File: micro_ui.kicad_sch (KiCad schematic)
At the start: 1 part

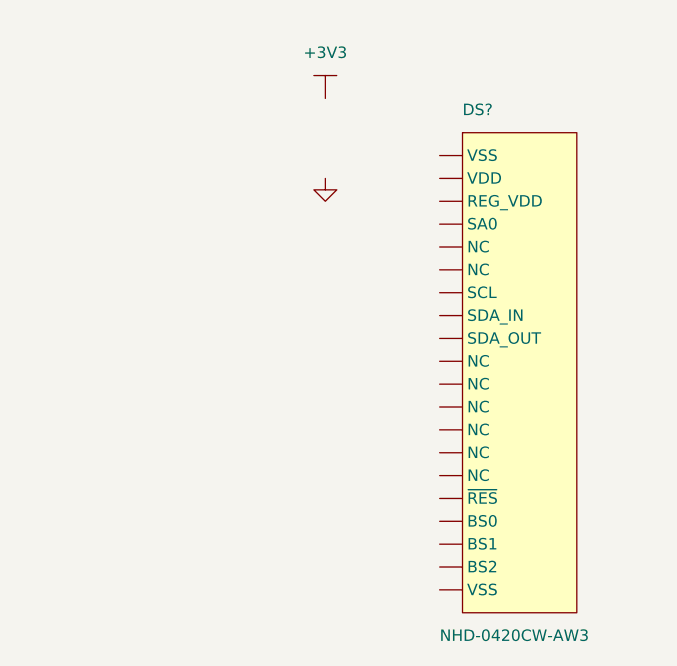
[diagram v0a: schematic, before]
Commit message: added symbols for i2c res and decoupling cap
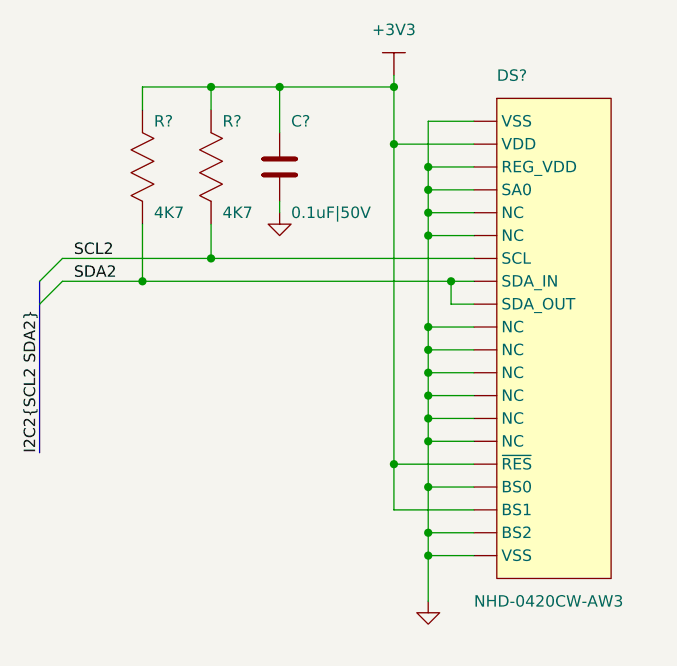
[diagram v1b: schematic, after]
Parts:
- added C?: 0.1uF|50V, symbol tbc:GCJ188R71H104KA12D
- added R? (x2): 4K7, symbol tbc:RC0603FR-074K7L
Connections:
- net +3V3: now also DS?.16 (~{RES}), DS?.18 (BS1), DS?.2 (VDD), C?.2, R?.2, R?.2
- net GND: now also DS?.1 (VSS), DS?.10 (DB3), DS?.11 (DB4), DS?.12 (DB5), DS?.13 (DB6), DS?.14 (DB7), DS?.15 (~{CS}), DS?.17 (BS0), DS?.19 (BS2), DS?.20 (VSS), DS?.3 (REG_VDD), DS?.4 (D_C), DS?.5 (R_W), DS?.6 (E), C?.1
- net SCL2: now reaches DS?.7 (DB0)
- net SCL2: now also R?.1
- net SDA2: now reaches DS?.8 (DB1)
- net SDA2: now also DS?.9 (DB2), R?.1
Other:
- moved on the sheet: DS?

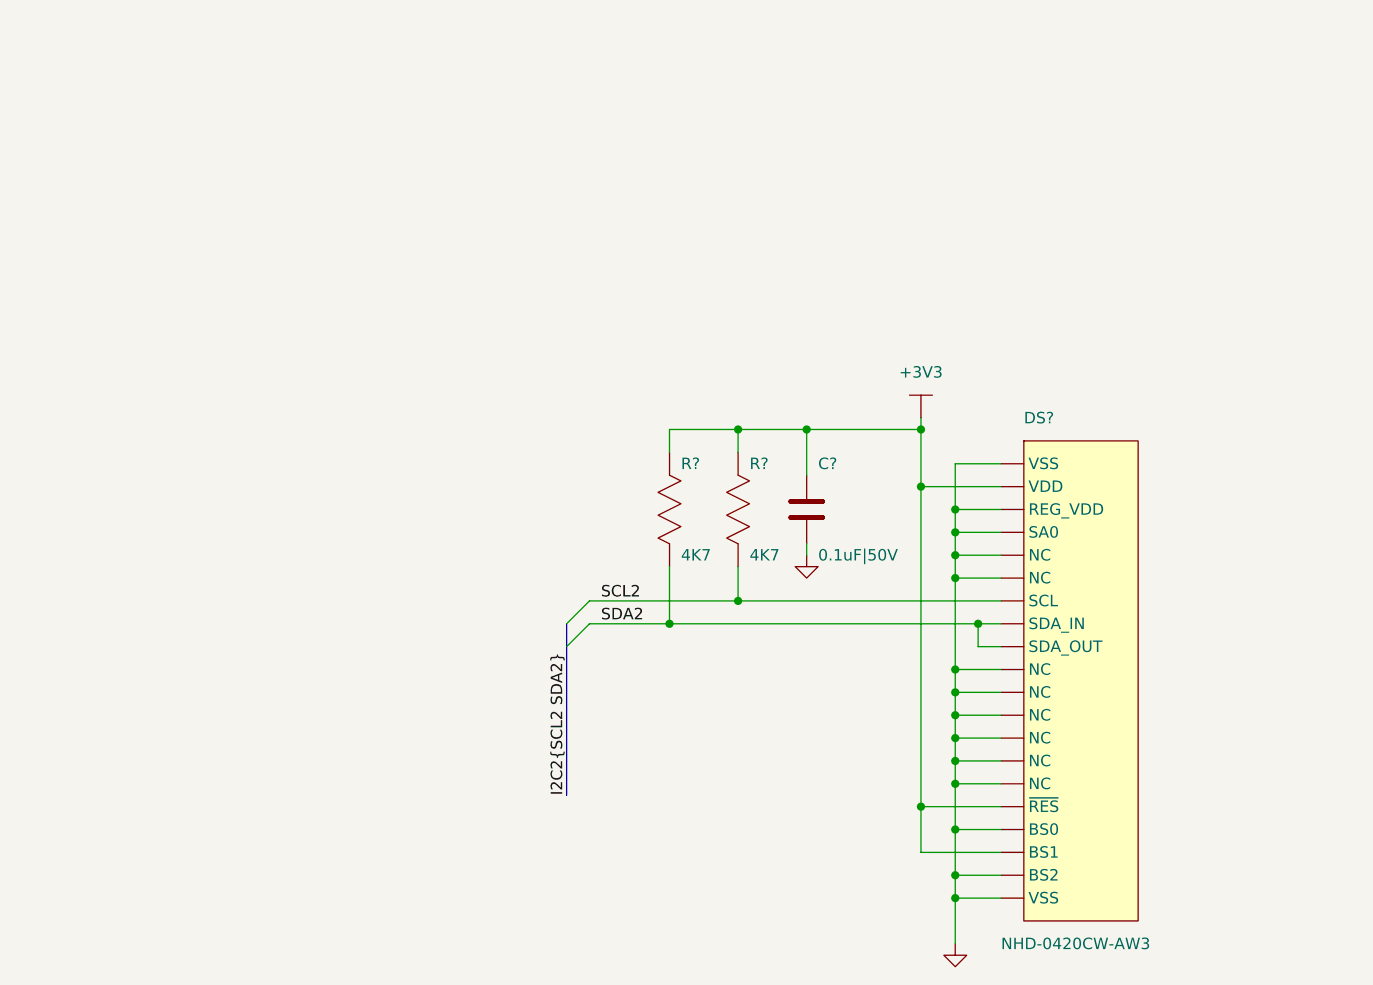
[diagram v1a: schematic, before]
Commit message: changed hierarchy, added symbols
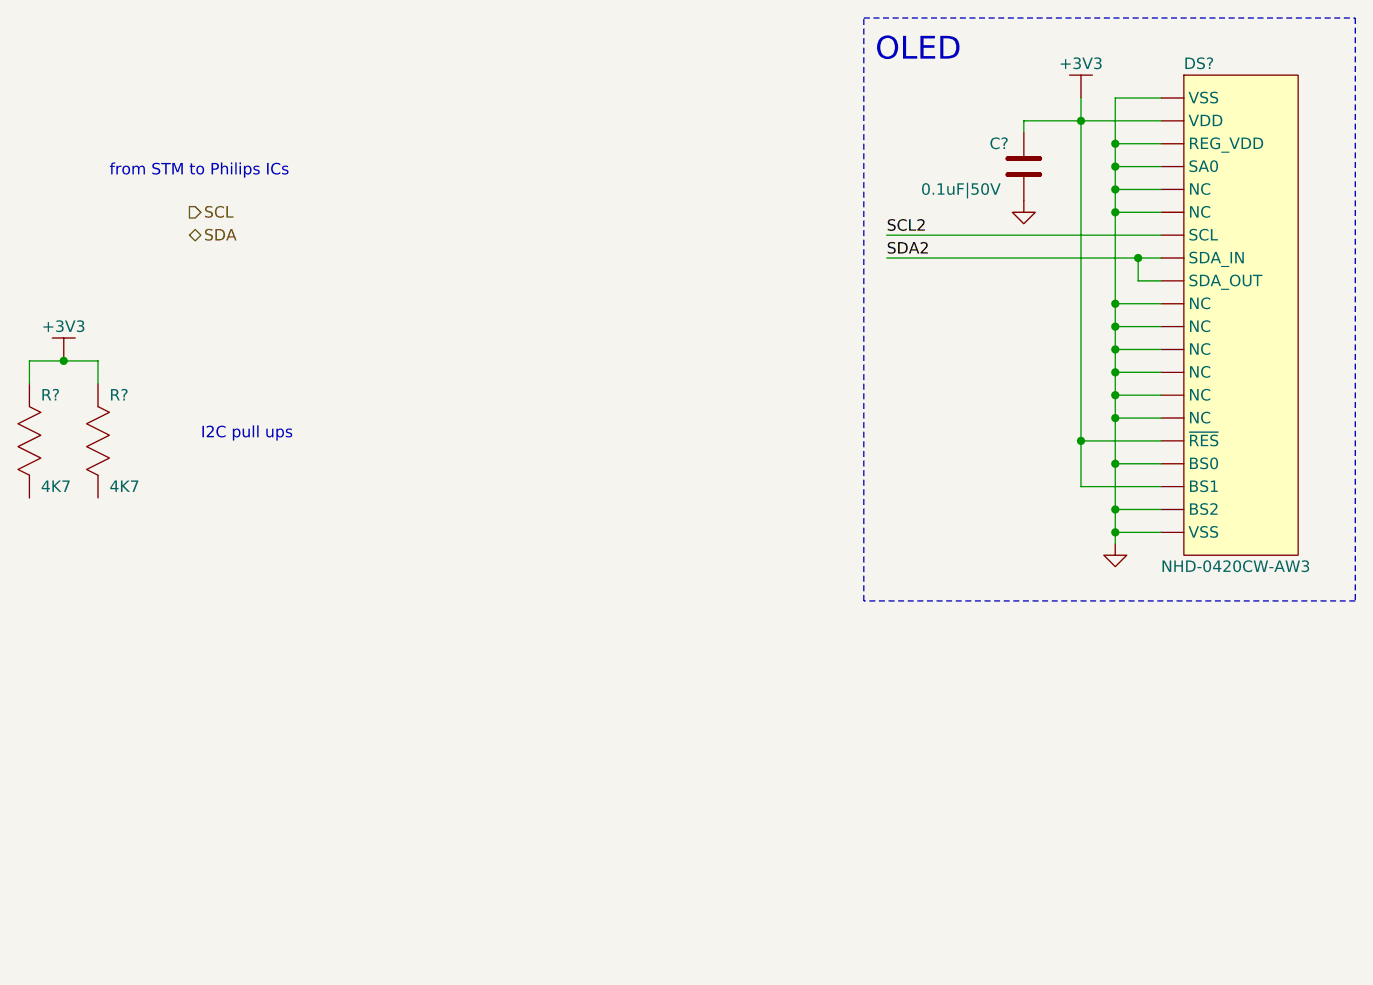
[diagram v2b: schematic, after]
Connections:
- net SCL2: no longer R?.1
- net SDA2: no longer R?.1
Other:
- note added: "I2C pull ups"
- note added: "OLED"
- note added: "from STM to Philips ICs"
- moved on the sheet: C?, DS?, R?

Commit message: added buses, title block info
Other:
- company: Wavelet Engineering Pty Ltd -> (none)
- title: Time Base Corrector -> Time Base Corrector and Video Scaler
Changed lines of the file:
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@@
   (paper "A4")
   (title_block
-    (title "Time Base Corrector")
+    (title "Time Base Corrector and Video Scaler")
     (date "2024-01-15")
     (rev "1")
-    (company "Wavelet Engineering Pty Ltd")
   )
   (junction (at 251.46 39.37) (diameter 0) (color 0 0 0 0)

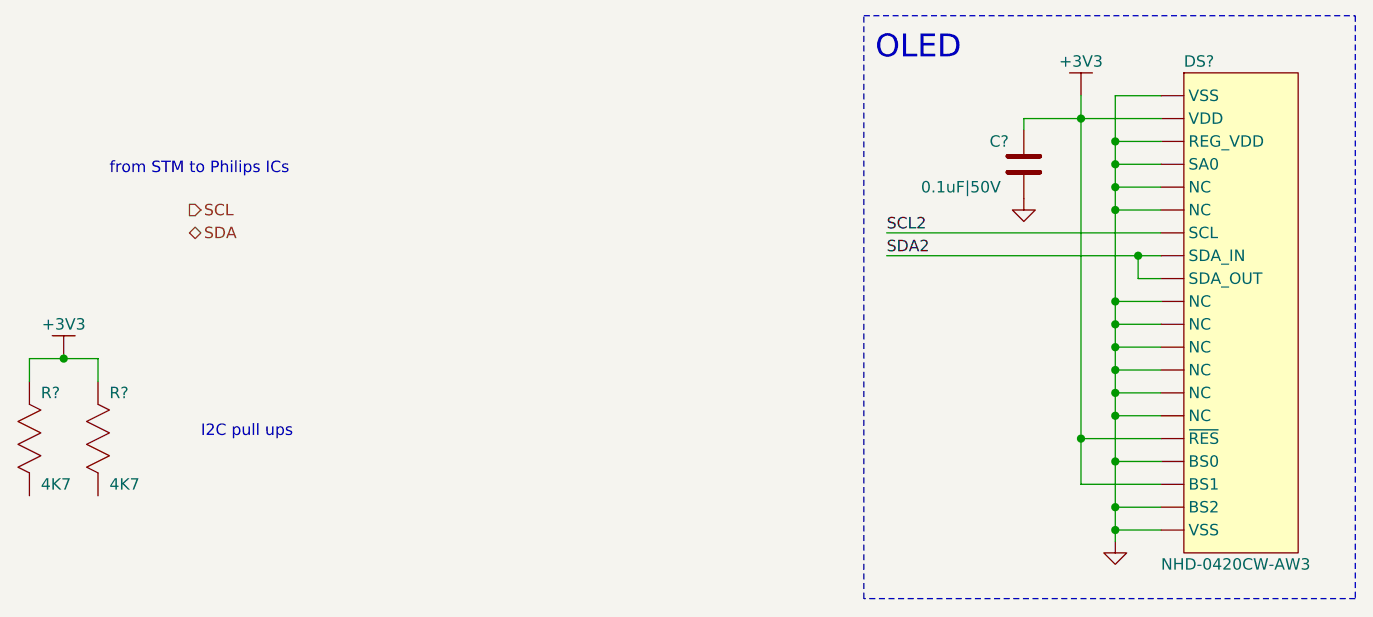
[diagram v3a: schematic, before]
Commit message: added frame memory symbol and updated schematic
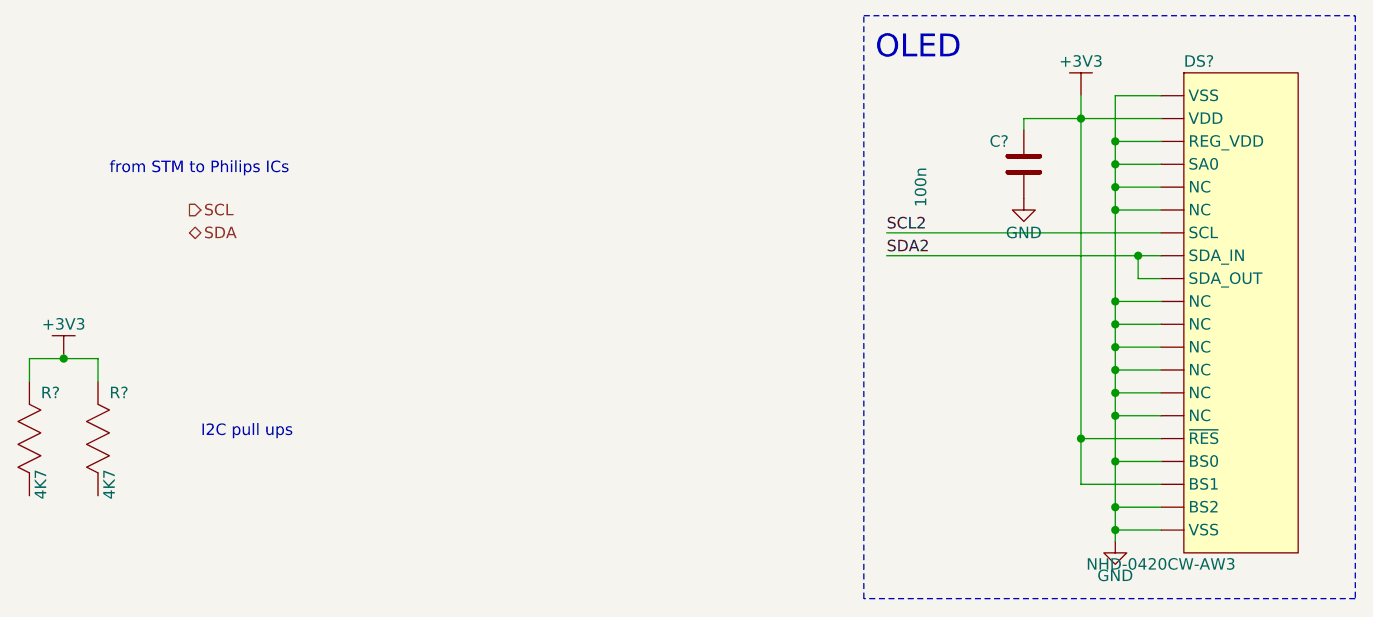
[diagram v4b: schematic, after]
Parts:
- C?: value 0.1uF|50V -> 100n; MPN GCJ188R71H104KA12D -> (none)
- DS?: MPN NHD-0420CW-AW3 -> (none)
- R? (x2): MPN RC0603FR-074K7L -> (none)
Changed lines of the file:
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@@
       (effects (font (size 1.27 1.27)) (justify right))
     )
-    (property "Value" "4K7" (at 132.08 69.85 90)
-      (effects (font (size 1.27 1.27)) (justify right))
+    (property "Value" "4K7" (at 132.08 69.85 0)
+      (effects (font (size 1.27 1.27)))
     )
     (property "Footprint" "" (at 138.43 81.28 0)
@@
     )
     (property "Datasheet" "https://www.yageo.com/upload/media/product/products/datasheet/rchip/PYu-RC_Group_51_RoHS_L_12.pdf" (at 143.51 81.28 0) (show_name)
-      (effects (font (size 1.27 1.27)) (justify left) hide)
-    )
-    (property "MPN" "RC0603FR-074K7L" (at 138.43 81.28 0) (show_name)
       (effects (font (size 1.27 1.27)) (justify left) hide)
     )
@@
       (effects (font (size 1.27 1.27)) (justify right))
     )
-    (property "Value" "4K7" (at 139.7 69.85 90)
-      (effects (font (size 1.27 1.27)) (justify right))
+    (property "Value" "4K7" (at 139.7 69.85 0)
+      (effects (font (size 1.27 1.27)))
     )
     (property "Footprint" "" (at 146.05 81.28 0)
@@
     )
     (property "Datasheet" "https://www.yageo.com/upload/media/product/products/datasheet/rchip/PYu-RC_Group_51_RoHS_L_12.pdf" (at 151.13 81.28 0) (show_name)
-      (effects (font (size 1.27 1.27)) (justify left) hide)
-    )
-    (property "MPN" "RC0603FR-074K7L" (at 146.05 81.28 0) (show_name)
       (effects (font (size 1.27 1.27)) (justify left) hide)
     )
@@
     )
     (property "Value" "NHD-0420CW-AW3" (at 256.54 78.74 0)
-      (effects (font (size 1.27 1.27)) (justify left))
+      (effects (font (size 1.27 1.27)))
     )
     (property "Footprint" "" (at 247.65 39.37 0)
@@
     )
     (property "Datasheet" "https://newhavendisplay.com/content/specs/NHD-0420CW-AW3.pdf" (at 241.3 87.63 0) (show_name)
-      (effects (font (size 1.27 1.27)) (justify left) hide)
-    )
-    (property "MPN" "NHD-0420CW-AW3" (at 241.3 82.55 0) (show_name)
       (effects (font (size 1.27 1.27)) (justify left) hide)
     )
@@
     )
     (property "Value" "GND" (at 241.3 41.91 0)
-      (effects (font (size 1.27 1.27)) hide)
+      (effects (font (size 1.27 1.27)))
     )
     (property "Footprint" "" (at 241.3 38.1 0)
@@
       (effects (font (size 1.27 1.27)) (justify right))
     )
-    (property "Value" "0.1uF|50V" (at 229.87 36.83 90)
-      (effects (font (size 1.27 1.27)) (justify right))
+    (property "Value" "100n" (at 229.87 36.83 0)
+      (effects (font (size 1.27 1.27)))
     )
     (property "Footprint" "" (at 252.73 34.29 0)
@@
     )
     (property "Datasheet" "https://au.mouser.com/datasheet/2/281/1/GCJ188R71H104KA12_02B-3140350.pdf" (at 254 48.26 0) (show_name)
-      (effects (font (size 1.27 1.27)) (justify left) hide)
-    )
-    (property "MPN" "GCJ188R71H104KA12D" (at 248.92 48.26 0) (show_name)
       (effects (font (size 1.27 1.27)) (justify left) hide)
     )
@@
     )
     (property "Value" "GND" (at 251.46 80.01 0)
-      (effects (font (size 1.27 1.27)) hide)
+      (effects (font (size 1.27 1.27)))
     )
     (property "Footprint" "" (at 251.46 76.2 0)
